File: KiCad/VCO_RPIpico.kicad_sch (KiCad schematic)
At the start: 79 parts, among them J1 AudioJack2, J2 Power Jack, SW1 LFO1/2, SW2 Select LFO WaveForm, SW3 Fire4, SW4 Fire3, SW5 Fire2, SW6 Fire1, SW7 Shift2/Save, SW8 Shift1 / Select Bank, U2 PT2399, U3 L7805

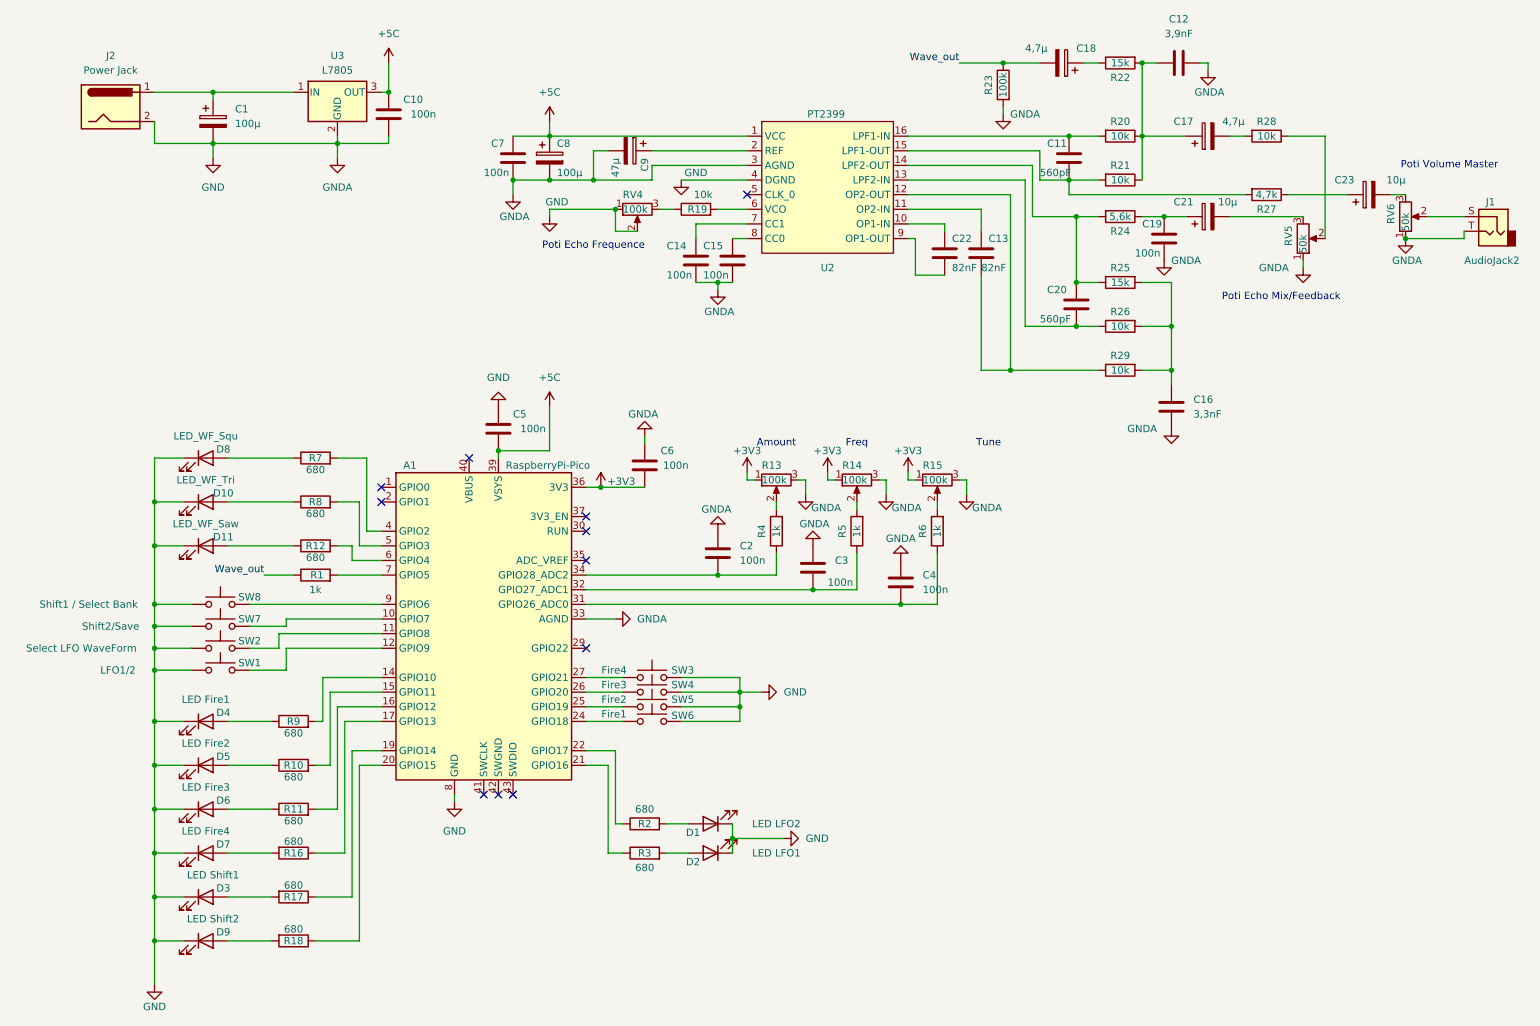
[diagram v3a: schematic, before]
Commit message: PCB neue Taster
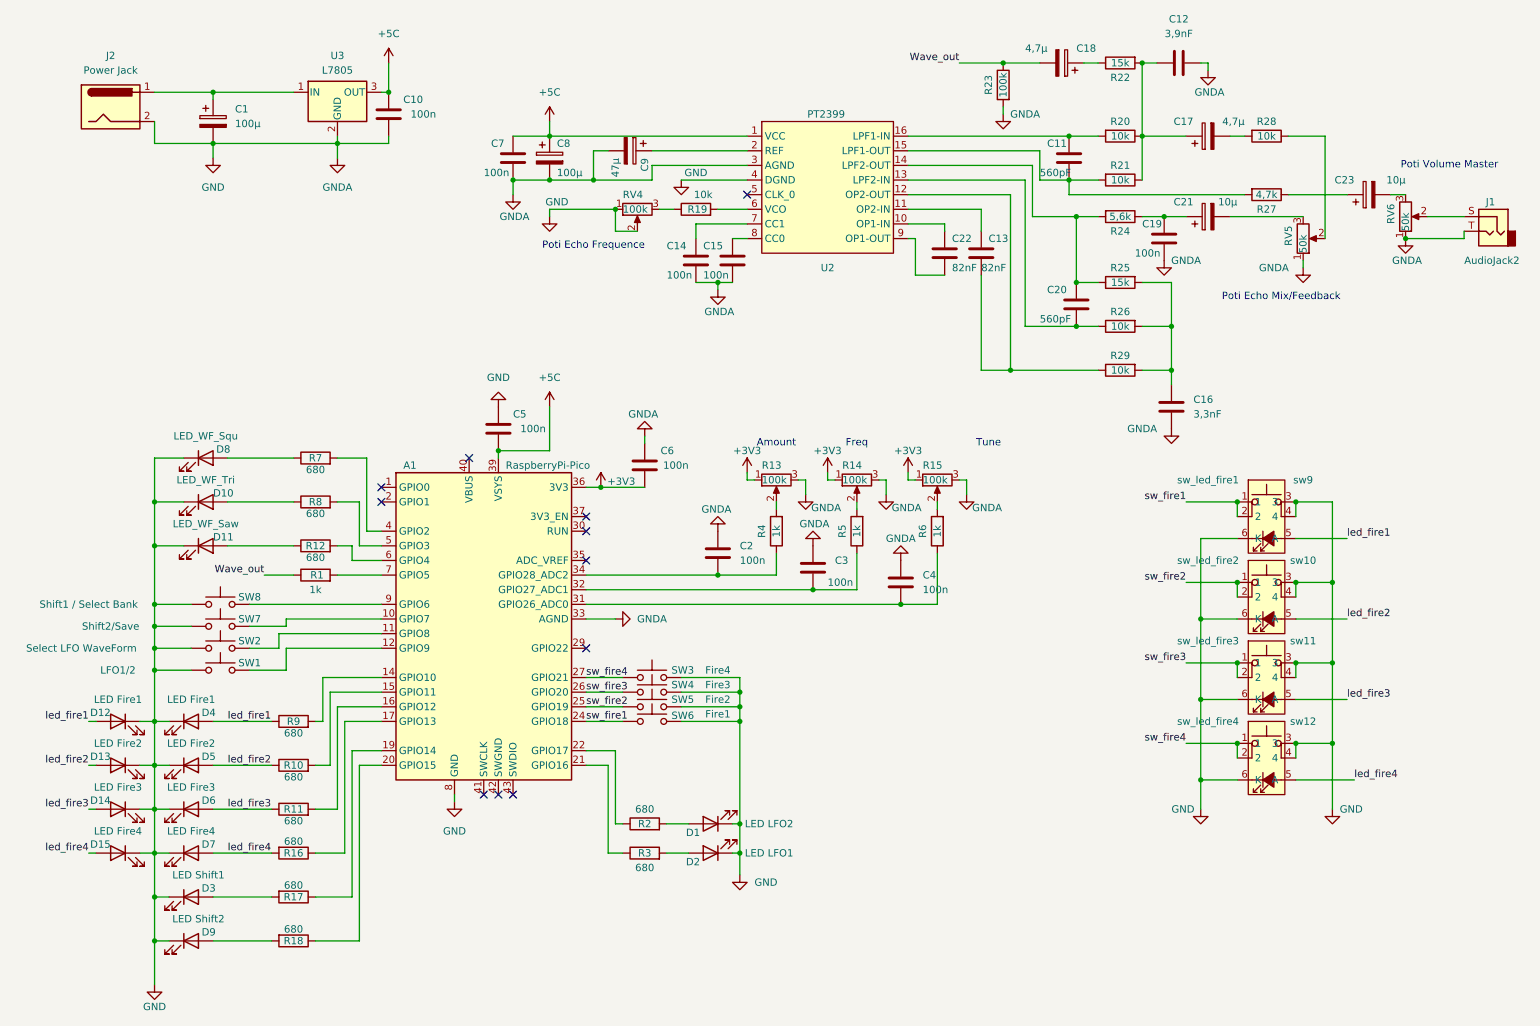
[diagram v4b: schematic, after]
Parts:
- added D12: LED Fire1, LED_SMD:LED_1206_3216Metric, symbol Device:LED
- added D13: LED Fire2, LED_SMD:LED_1206_3216Metric, symbol Device:LED
- added D14: LED Fire3, LED_SMD:LED_1206_3216Metric, symbol Device:LED
- added D15: LED Fire4, LED_SMD:LED_1206_3216Metric, symbol Device:LED
- added sw10: sw_led_fire2, switches:Multimec Switch THT, symbol eigene_24:switch_led
- added sw11: sw_led_fire3, switches:Multimec Switch THT, symbol eigene_24:switch_led
- added sw12: sw_led_fire4, switches:Multimec Switch THT, symbol eigene_24:switch_led
- added sw9: sw_led_fire1, switches:Multimec Switch THT, symbol eigene_24:switch_led
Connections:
- net GND: now also D12.1 (K), D13.1 (K), D14.1 (K), D15.1 (K), sw10.3, sw10.4, sw10.6 (K), sw11.3, sw11.4, sw11.6 (K), sw12.3, sw12.4, sw12.6 (K), sw9.3, sw9.4, sw9.6 (K)
- net led_fire3: now reaches D6.2 (A), R11.1
- net led_fire3: now also D14.2 (A), sw11.5 (A)
- net sw_fire4: now reaches A1.27 (GPIO21), SW3.1
- net sw_fire4: now also sw12.1, sw12.2
- net led_fire1: now reaches D4.2 (A), R9.1
- net led_fire1: now also D12.2 (A), sw9.5 (A)
- net led_fire2: now reaches D5.2 (A), R10.1
- net led_fire2: now also D13.2 (A), sw10.5 (A)
- net sw_fire1: now reaches A1.24 (GPIO18), SW6.1
- net sw_fire1: now also sw9.1, sw9.2
- net sw_fire2: now reaches A1.25 (GPIO19), SW5.1
- net sw_fire2: now also sw10.1, sw10.2
- net sw_fire3: now reaches A1.26 (GPIO20), SW4.1
- net sw_fire3: now also sw11.1, sw11.2
- net led_fire4: now reaches D7.2 (A), R16.2
- net led_fire4: now also D15.2 (A), sw12.5 (A)
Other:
- moved on the sheet: D3, D4, D5, D6, D7, D9

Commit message: PCB fertig, Gerber Export
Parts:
- C19: value 100n -> 10n
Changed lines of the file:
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@@
 	)
 	(junction
-		(at 224.79 115.57)
+		(at 180.34 64.77)
 		(diameter 0)
 		(color 0 0 0 0)
 	)
 	(junction
-		(at 113.03 45.72)
+		(at 224.79 115.57)
 		(diameter 0)
 		(color 0 0 0 0)
 	)
 	(junction
-		(at 138.43 162.56)
+		(at 113.03 45.72)
 		(diameter 0)
 		(color 0 0 0 0)
 	)
 	(junction
-		(at 185.42 78.74)
+		(at 138.43 162.56)
 		(diameter 0)
 		(color 0 0 0 0)
@@
 	(wire
 		(pts
-			(xy 185.42 78.74) (xy 200.66 78.74)
+			(xy 180.34 78.74) (xy 200.66 78.74)
 		)
 		(stroke
@@
 	(wire
 		(pts
-			(xy 167.64 55.88) (xy 168.91 55.88)
+			(xy 168.91 55.88) (xy 167.64 55.88)
 		)
 		(stroke
@@
 	(wire
 		(pts
-			(xy 180.34 78.74) (xy 185.42 78.74)
-		)
-		(stroke
-			(width 0)
-			(type default)
-		)
-	)
-	(wire
-		(pts
 			(xy 241.3 129.54) (xy 241.3 115.57)
 		)
@@
 	(wire
 		(pts
-			(xy 168.91 62.23) (xy 168.91 55.88)
+			(xy 168.91 64.77) (xy 168.91 55.88)
 		)
 		(stroke
@@
 	(wire
 		(pts
+			(xy 180.34 64.77) (xy 180.34 78.74)
+		)
+		(stroke
+			(width 0)
+			(type default)
+		)
+	)
+	(wire
+		(pts
 			(xy 36.83 170.18) (xy 39.37 170.18)
 		)
@@
 	(wire
 		(pts
+			(xy 180.34 64.77) (xy 185.42 64.77)
+		)
+		(stroke
+			(width 0)
+			(type default)
+		)
+	)
+	(wire
+		(pts
 			(xy 241.3 129.54) (xy 234.95 129.54)
 		)
@@
 	(wire
 		(pts
-			(xy 173.99 62.23) (xy 168.91 62.23)
+			(xy 173.99 64.77) (xy 168.91 64.77)
+		)
+		(stroke
+			(width 0)
+			(type default)
+		)
+	)
+	(wire
+		(pts
+			(xy 173.99 64.77) (xy 173.99 62.23)
 		)
 		(stroke
@@
 	(wire
 		(pts
-			(xy 180.34 62.23) (xy 180.34 78.74)
+			(xy 180.34 62.23) (xy 180.34 64.77)
 		)
 		(stroke
@@
 	(wire
 		(pts
+			(xy 185.42 64.77) (xy 185.42 48.26)
+		)
+		(stroke
+			(width 0)
+			(type default)
+		)
+	)
+	(wire
+		(pts
 			(xy 234.95 121.92) (xy 243.84 121.92)
 		)
@@
 	(wire
 		(pts
-			(xy 185.42 78.74) (xy 185.42 48.26)
-		)
-		(stroke
-			(width 0)
-			(type default)
-		)
-	)
-	(wire
-		(pts
 			(xy 218.44 107.95) (xy 224.79 107.95)
 		)
@@
 		(on_board yes)
 		(dnp no)
-		(fields_autoplaced yes)
 		(property "Reference" "C2"
-			(at 138.43 109.2199 0)
+			(at 136.398 108.204 0)
 			(effects
 				(font
@@
 		)
 		(property "Value" "100n"
-			(at 138.43 111.7599 0)
+			(at 135.89 112.776 0)
 			(effects
 				(font
@@
 		(on_board yes)
 		(dnp no)
-		(fields_autoplaced yes)
 		(property "Reference" "C4"
-			(at 170.18 114.2999 0)
+			(at 167.64 113.538 0)
 			(effects
 				(font
@@
 		)
 		(property "Value" "100n"
-			(at 170.18 116.8399 0)
+			(at 167.894 118.11 0)
 			(effects
 				(font
@@
 		(dnp no)
 		(property "Reference" "C3"
-			(at 154.94 111.7599 0)
+			(at 152.654 110.744 0)
 			(effects
 				(font
@@
 		)
 		(property "Value" "100n"
-			(at 153.67 115.57 0)
+			(at 152.4 115.316 0)
 			(effects
 				(font
@@
 			)
 		)
-		(property "Value" "100n"
+		(property "Value" "10n"
 			(at 207.01 58.42 0)
 			(effects

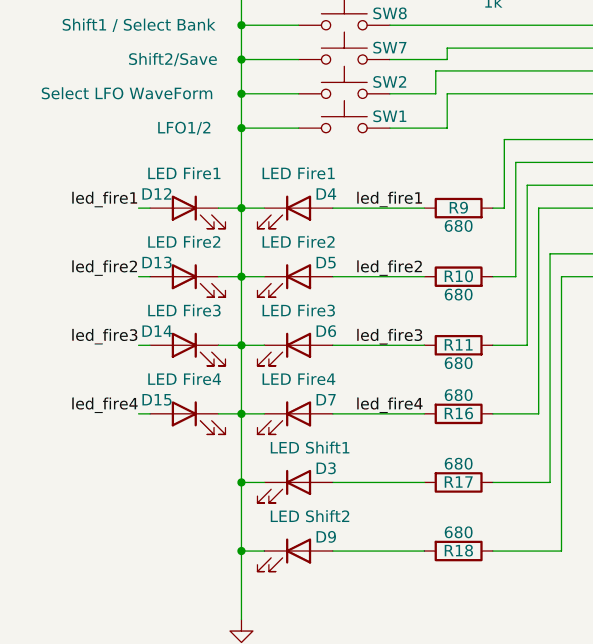
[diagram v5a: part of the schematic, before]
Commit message: zusätzliche LEDs unter die kleinen FIre-Button
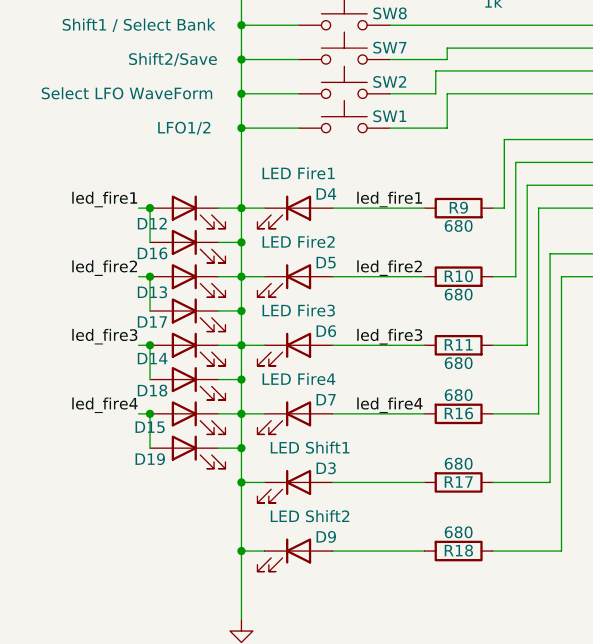
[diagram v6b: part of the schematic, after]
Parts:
- added D16: LED Fire1, LED_SMD:LED_1206_3216Metric, symbol Device:LED
- added D17: LED Fire2, LED_SMD:LED_1206_3216Metric, symbol Device:LED
- added D18: LED Fire3, LED_SMD:LED_1206_3216Metric, symbol Device:LED
- added D19: LED Fire4, LED_SMD:LED_1206_3216Metric, symbol Device:LED
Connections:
- net GND: now also D16.1 (K), D17.1 (K), D18.1 (K), D19.1 (K)
- net led_fire1: now also D16.2 (A)
- net led_fire2: now also D17.2 (A)
- net led_fire3: now also D18.2 (A)
- net led_fire4: now also D19.2 (A)

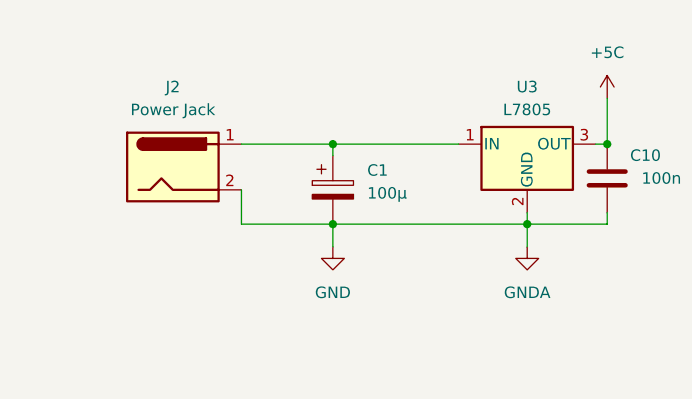
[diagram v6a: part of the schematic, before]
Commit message: Kicad Schottkydiode added
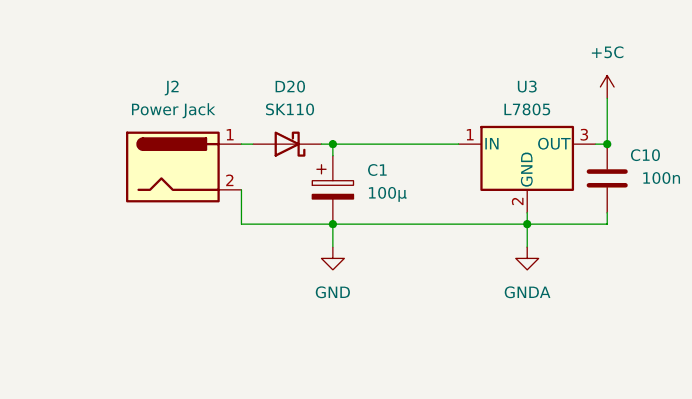
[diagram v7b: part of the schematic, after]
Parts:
- added D20: SK110, Diode_SMD:D_SMA-SMB_Universal_Handsoldering, symbol Device:D_Schottky
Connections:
- net at C1.1, U3.1 (IN): now also D20.1 (K); no longer J2.1
- new net: D20.2 (A), J2.1
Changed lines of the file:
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@@
 	(wire
 		(pts
-			(xy 219.71 25.4) (xy 219.71 26.67)
+			(xy 38.1 30.48) (xy 36.83 30.48)
 		)
 		(stroke
@@
 	(wire
 		(pts
-			(xy 36.83 30.48) (xy 46.99 30.48)
+			(xy 219.71 25.4) (xy 219.71 26.67)
 		)
 		(stroke
@@
 	(wire
 		(pts
+			(xy 45.72 30.48) (xy 46.99 30.48)
+		)
+		(stroke
+			(width 0)
+			(type default)
+		)
+	)
+	(wire
+		(pts
 			(xy 241.3 143.51) (xy 241.3 129.54)
 		)
@@
 					(unit 1)
 				)
+			)
+		)
+	)
+	(symbol
+		(lib_id "Device:D_Schottky")
+		(at 41.91 30.48 180)
+		(unit 1)
+		(exclude_from_sim no)
+		(in_bom yes)
+		(on_board yes)
+		(dnp no)
+		(fields_autoplaced yes)
+		(property "Reference" "D20"
+			(at 42.2275 24.13 0)
+			(effects
+				(font
+					(size 1.27 1.27)
+				)
+			)
+		)
+		(property "Value" "SK110"
+			(at 42.2275 26.67 0)
+			(effects
+				(font
+					(size 1.27 1.27)
+				)
+			)
+		)
+		(property "Footprint" "Diode_SMD:D_SMA-SMB_Universal_Handsoldering"
+			(at 41.91 30.48 0)
+			(effects
+				(font
+					(size 1.27 1.27)
+				)
+				(hide yes)
+			)
+		)
+		(property "Datasheet" "~"
+			(at 41.91 30.48 0)
+			(effects
+				(font
+					(size 1.27 1.27)
+				)
+				(hide yes)
+			)
+		)
+		(property "Description" "Schottky diode"
+			(at 41.91 30.48 0)
+			(effects
+				(font
+					(size 1.27 1.27)
+				)
+				(hide yes)
+			)
+		)
+		(pin "1"
+		)
+		(pin "2"
+		)
+		(instances
+			(project ""
+				(path "/0d855e99-162c-4989-8fe3-f98154ec6843"
+					(reference "D20")
+					(unit 1)
+				)

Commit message: Kicad kleine Änderung
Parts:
- removed R13, R14, R15, RV4: 100k, Potentiometer_THT:Potentiometer_Alps_RK09K_Single_Vertical, symbol Device:R_Potentiometer
- removed RV5, RV6: 50k, Potentiometer_THT:Potentiometer_Alps_RK09K_Single_Vertical, symbol Device:R_Potentiometer
- added R13, R14, R15, RV4, RV5, RV6: 100k, Potentiometer_THT:Potentiometer_Alps_RK09K_Single_Vertical, symbol Device:R_Potentiometer_MountingPin
- J1: value AudioJack2 -> AudioJack
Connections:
- net +3V3: now also R13.1, R14.1, R15.1
- net GND: now also R13.3, R13.MP (MountPin), R14.3, R14.MP (MountPin), R15.3, R15.MP (MountPin), RV4.1, RV4.2, RV4.MP (MountPin), RV5.1, RV5.MP (MountPin), RV6.1, RV6.MP (MountPin)
- net at R6.2: now also R15.2
- net at R5.2: now also R14.2
- net at C23.2: now also RV6.3
- net at R28.1: now also RV5.2
- net at J1.S: now also RV6.2
- net at C21.2: now also RV5.3
- net at R19.1: now also RV4.3
- net at R4.2: now also R13.2
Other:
- moved on the sheet: R4, R5, R6
